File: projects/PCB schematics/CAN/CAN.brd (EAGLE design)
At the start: 160 x 100 mm, 0 parts

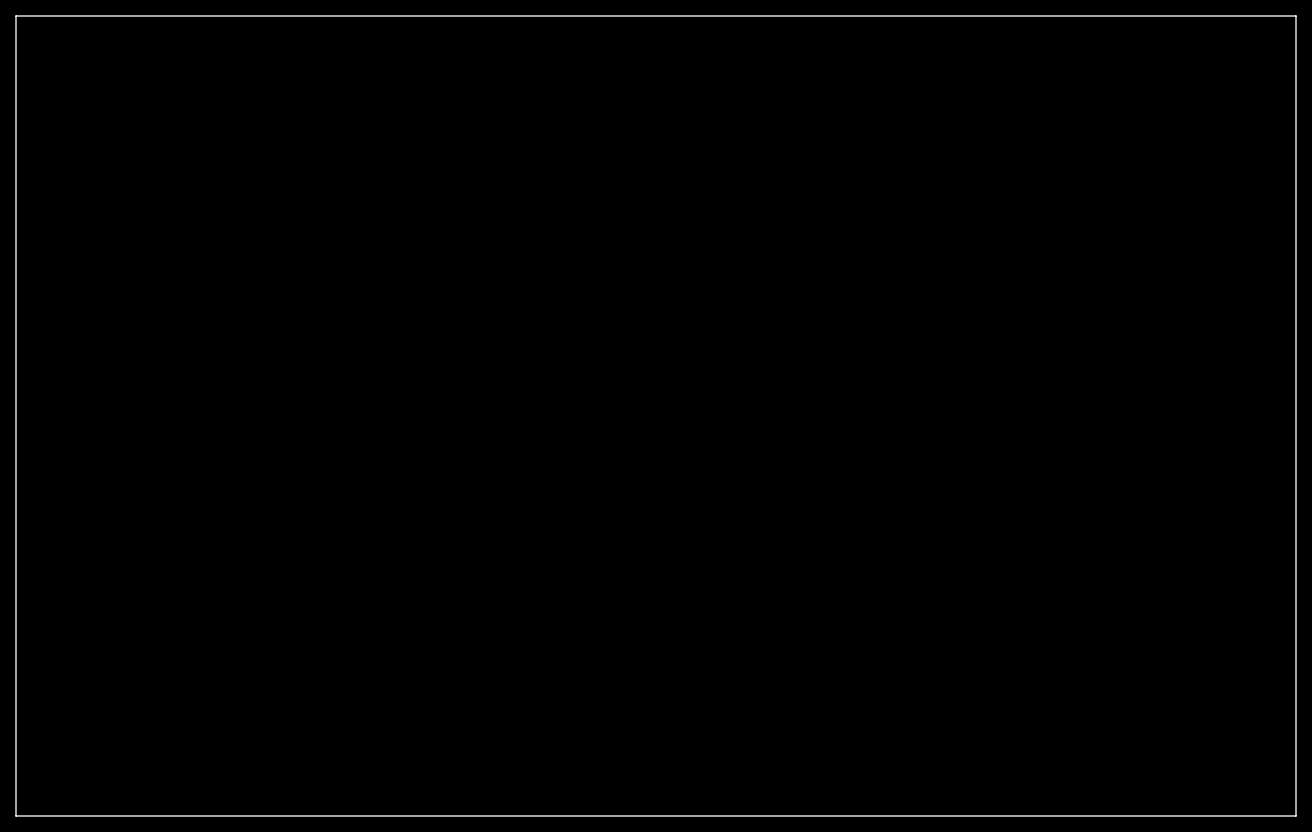
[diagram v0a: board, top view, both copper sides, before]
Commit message: CAN - Initial draft.
Vertical connectors chosen. Several options should be compliant with this PCB footprint.
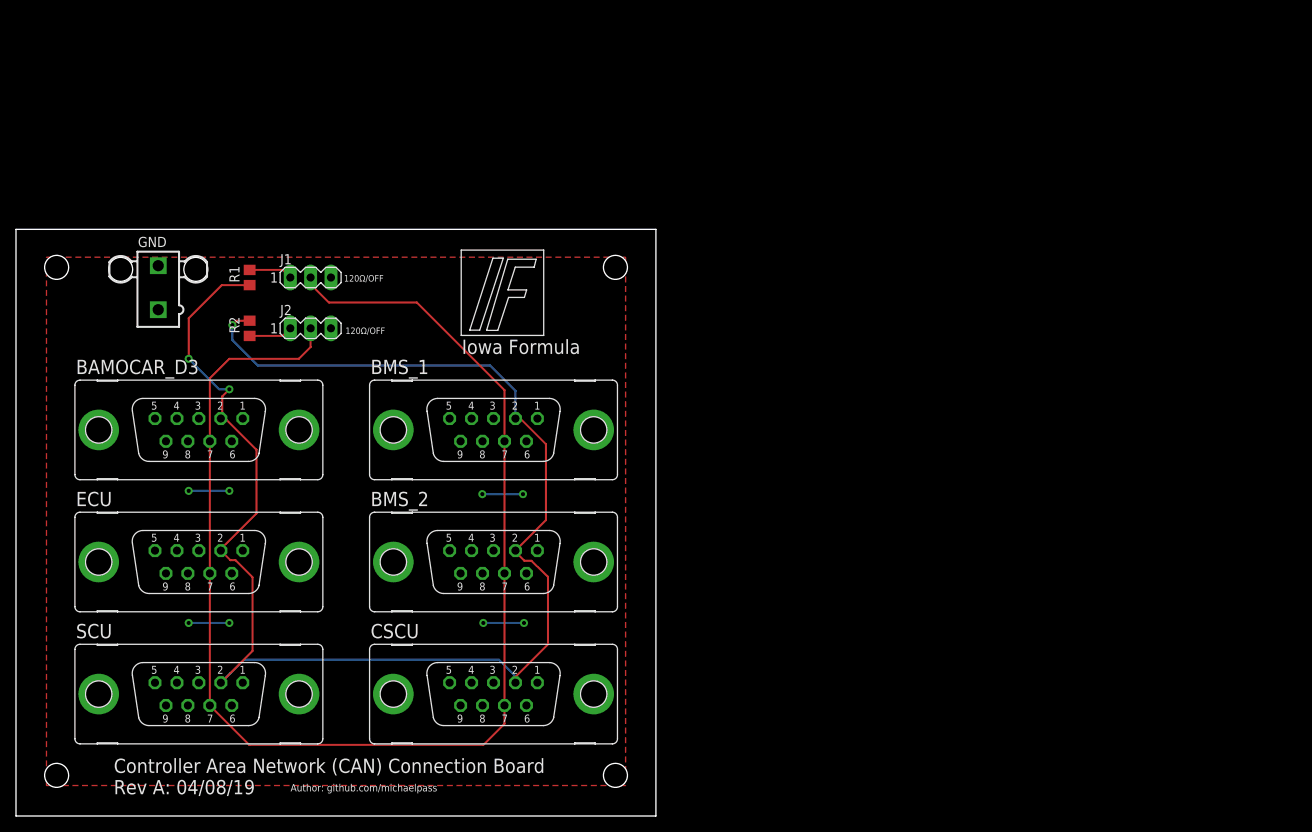
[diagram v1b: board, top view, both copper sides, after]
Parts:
- added BAMOCAR_D3, BMS_1, BMS_2, CSCU, ECU, SCU: (no value), con-subd:F09VP
- added GND: 5566-2, con-molex:5566-2
- added J1, J2: (no value), con-lstb:MA03-1
- added R1, R2: (no value), rcl:R0805
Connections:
- new net CANH: BAMOCAR_D3.7, BMS_1.7, BMS_2.7, CSCU.7, ECU.7, J1.2, J2.2, SCU.7
- new net CANL: BAMOCAR_D3.2, BMS_1.2, BMS_2.2, CSCU.2, ECU.2, R1.2, R2.2, SCU.2
- new net GND: BAMOCAR_D3.3, BAMOCAR_D3.6, BMS_1.3, BMS_1.6, BMS_2.3, BMS_2.6, CSCU.3, CSCU.6, ECU.3, ECU.6, GND.1, GND.2, SCU.3, SCU.6
- new net N$2: J2.3
- new net N$3: J2.1, R2.1
- new net N$4: J1.1, R1.1
- new net N$6: J1.3
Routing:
- net CANL: track 0.00 -> 191.8 mm, vias 0 -> 3
- net CANH: track 0.00 -> 169.7 mm
- net GND: track 0.00 -> 20.3 mm, vias 0 -> 8
- net N$4: track 0.00 -> 5.47 mm
- net N$3: track 0.00 -> 5.47 mm
- added copper zone on layer 1, net GND
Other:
- board size 160 x 100 mm -> 80 x 73.3 mm
- board text added: "120Ω/OFF"
- board text added: "Author: github.com/michaelpass"
- board text added: "Controller Area Network (CAN) Connection Board Rev A: 04/08/19"
- board text added: "Iowa Formula"

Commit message: CAN - Added in resistor values.
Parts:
- R1, R2: value (none) -> 120
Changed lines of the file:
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@@
 <attribute name="VALUE" x="33.02" y="58.039" size="1.27" layer="27" ratio="10"/>
 </element>
-<element name="R1" library="rcl" library_urn="urn:adsk.eagle:library:334" package="R0805" package3d_urn="urn:adsk.eagle:package:23553/2" value="" x="29.21" y="67.31" smashed="yes" rot="R270">
+<element name="R1" library="rcl" library_urn="urn:adsk.eagle:library:334" package="R0805" package3d_urn="urn:adsk.eagle:package:23553/2" value="120" x="29.21" y="67.31" smashed="yes" rot="R270">
 <attribute name="NAME" x="27.94" y="66.675" size="1.27" layer="25" rot="R90"/>
 <attribute name="SPICEPREFIX" value="R" x="29.21" y="67.31" size="1.778" layer="27" rot="R270" display="off"/>
 <attribute name="VALUE" x="26.67" y="67.945" size="1.27" layer="27" rot="R270"/>
 </element>
-<element name="R2" library="rcl" library_urn="urn:adsk.eagle:library:334" package="R0805" package3d_urn="urn:adsk.eagle:package:23553/2" value="" x="29.21" y="60.96" smashed="yes" rot="R90">
+<element name="R2" library="rcl" library_urn="urn:adsk.eagle:library:334" package="R0805" package3d_urn="urn:adsk.eagle:package:23553/2" value="120" x="29.21" y="60.96" smashed="yes" rot="R90">
 <attribute name="NAME" x="27.94" y="60.325" size="1.27" layer="25" rot="R90"/>
 <attribute name="SPICEPREFIX" value="R" x="29.21" y="60.96" size="1.778" layer="27" rot="R90" display="off"/>

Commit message: TSAL - Resizing.
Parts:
- moved SCU 15.3 mm to (33.0, 26.7)
- moved BAMOCAR_D3 15.3 mm to (33.0, 59.7)
- moved ECU 15.3 mm to (33.0, 43.2)
- moved J2 15.3 mm to (47.0, 72.4)
- moved CSCU 15.3 mm to (69.8, 26.7)
- moved J1 15.3 mm to (47.0, 78.7)
- moved BMS_1 15.3 mm to (69.8, 59.7)
- moved BMS_2 15.3 mm to (69.8, 43.2)
- moved R2 15.3 mm to (39.4, 72.4)
- moved GND 15.3 mm to (27.9, 77.5)
- moved R1 15.3 mm to (39.4, 78.7)
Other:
- board size 80 x 73.3 mm -> 99.1 x 99.1 mm

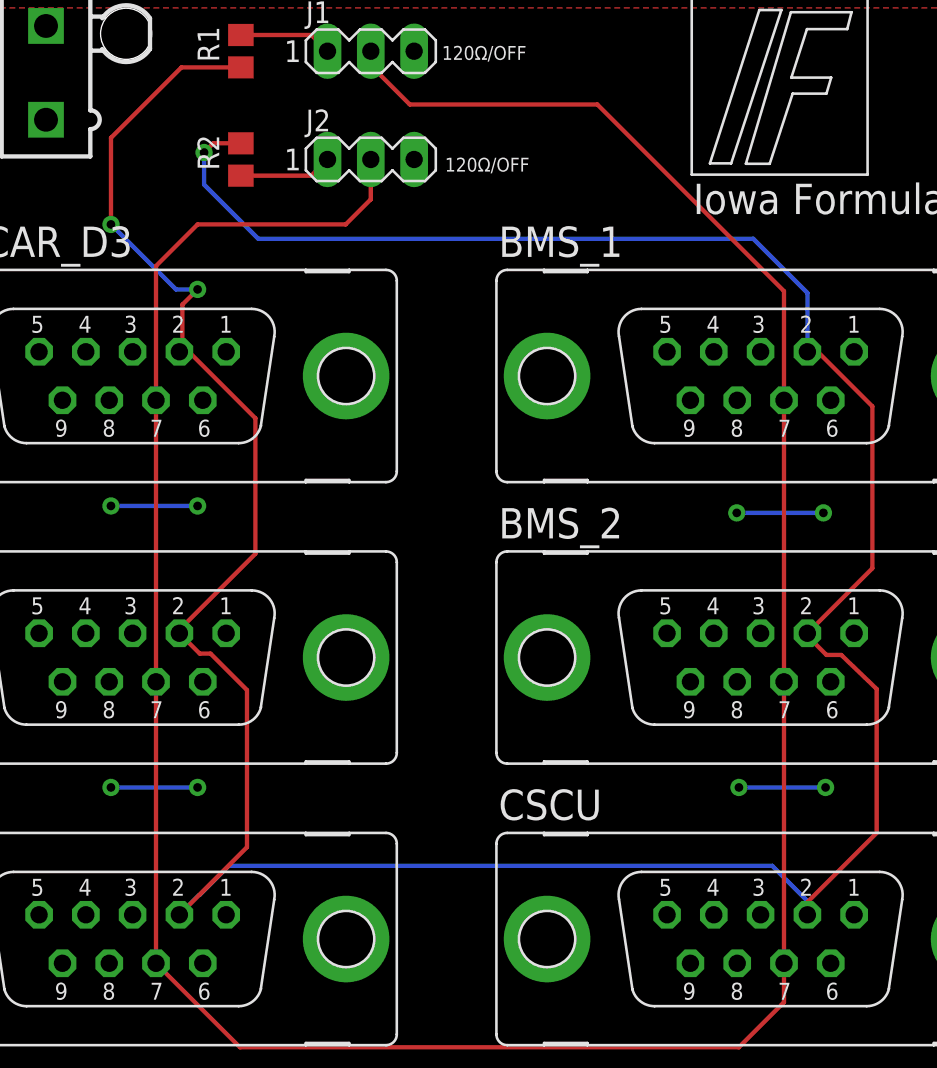
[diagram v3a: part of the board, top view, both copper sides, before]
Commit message: CAN - Further distancing of CAN_H/CAN_L routing.
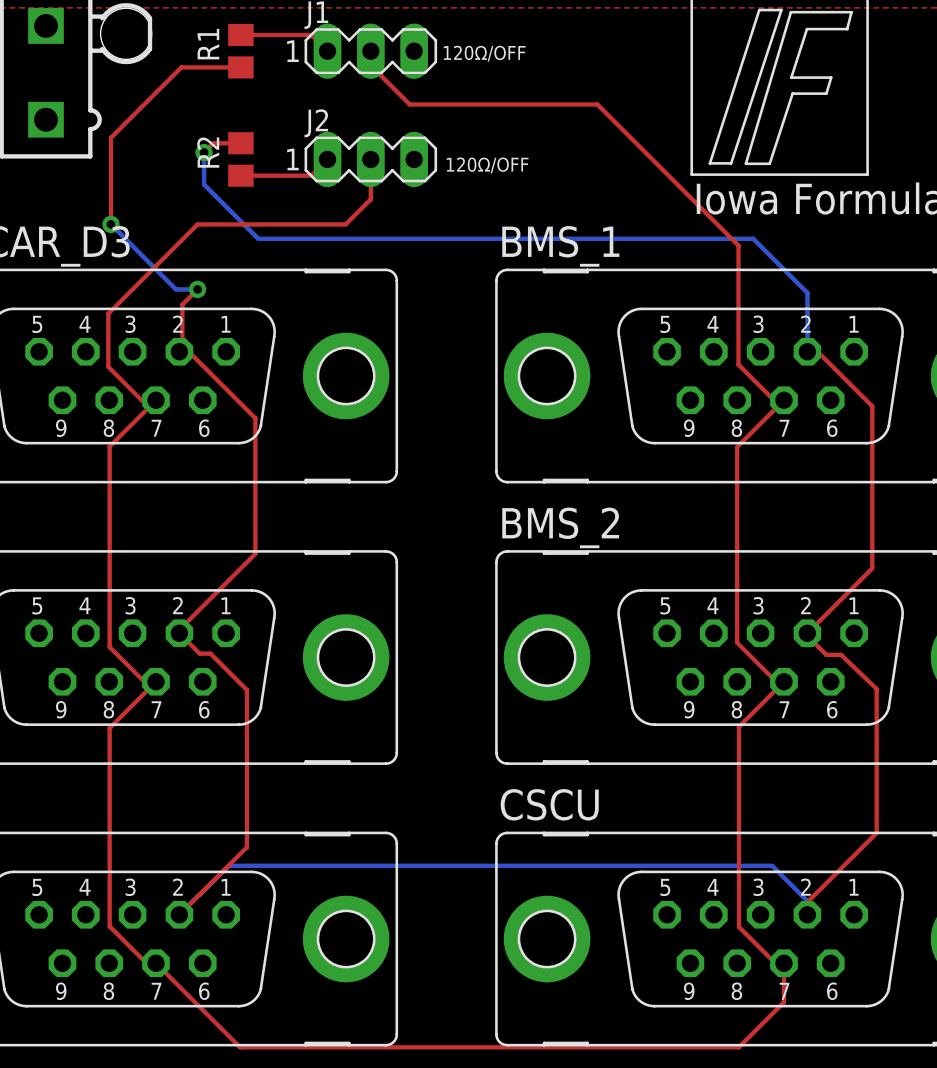
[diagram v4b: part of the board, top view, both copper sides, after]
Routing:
- net GND: track 20.3 -> 0.00 mm, vias 8 -> 0
- net CANH: track 169.7 -> 183.1 mm
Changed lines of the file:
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@@
 <contactref element="BMS_2" pad="6"/>
 <contactref element="BMS_2" pad="3"/>
-<via x="36.83" y="52.07" extent="1-16" drill="0.508"/>
-<via x="31.75" y="52.07" extent="1-16" drill="0.508"/>
-<wire x1="31.75" y1="52.07" x2="36.83" y2="52.07" width="0.254" layer="16"/>
-<via x="73.66" y="35.56" extent="1-16" drill="0.508"/>
-<via x="68.58" y="35.56" extent="1-16" drill="0.508"/>
-<wire x1="68.58" y1="35.56" x2="73.66" y2="35.56" width="0.254" layer="16"/>
-<via x="73.533" y="51.6636" extent="1-16" drill="0.508"/>
-<via x="68.453" y="51.6636" extent="1-16" drill="0.508"/>
-<wire x1="68.453" y1="51.6636" x2="73.533" y2="51.6636" width="0.254" layer="16"/>
-<via x="36.83" y="35.56" extent="1-16" drill="0.508"/>
-<via x="31.75" y="35.56" extent="1-16" drill="0.508"/>
-<wire x1="31.75" y1="35.56" x2="36.83" y2="35.56" width="0.254" layer="16"/>
 </signal>
 <signal name="N$2">
@@
 <contactref element="SCU" pad="7"/>
 <contactref element="CSCU" pad="7"/>
-<wire x1="34.3916" y1="58.2676" x2="34.3916" y2="41.7576" width="0.254" layer="1"/>
-<wire x1="34.3916" y1="41.7576" x2="34.3916" y2="25.2476" width="0.254" layer="1"/>
-<wire x1="71.2216" y1="41.7576" x2="71.2216" y2="58.2676" width="0.254" layer="1"/>
-<wire x1="71.2216" y1="25.2476" x2="71.2216" y2="41.7576" width="0.254" layer="1"/>
-<wire x1="34.3916" y1="58.2676" x2="34.3916" y2="66.1416" width="0.254" layer="1"/>
-<wire x1="34.3916" y1="66.1416" x2="36.83" y2="68.58" width="0.254" layer="1"/>
+<wire x1="34.3916" y1="58.2676" x2="31.6738" y2="55.5498" width="0.254" layer="1"/>
+<wire x1="31.6738" y1="55.5498" x2="31.6738" y2="43.7896" width="0.254" layer="1"/>
+<wire x1="33.7058" y1="41.7576" x2="34.3916" y2="41.7576" width="0.254" layer="1"/>
+<wire x1="33.7058" y1="41.7576" x2="31.6738" y2="43.7896" width="0.254" layer="1"/>
+<wire x1="34.3916" y1="41.7576" x2="31.6738" y2="39.0398" width="0.254" layer="1"/>
+<wire x1="31.6738" y1="39.0398" x2="31.6738" y2="27.4066" width="0.254" layer="1"/>
+<wire x1="33.8328" y1="25.2476" x2="31.6738" y2="27.4066" width="0.254" layer="1"/>
+<wire x1="33.8328" y1="25.2476" x2="34.3916" y2="25.2476" width="0.254" layer="1"/>
+<wire x1="71.2216" y1="41.7576" x2="70.7644" y2="41.7576" width="0.254" layer="1"/>
+<wire x1="70.7644" y1="41.7576" x2="68.4784" y2="44.0436" width="0.254" layer="1"/>
+<wire x1="68.4784" y1="55.5244" x2="68.4784" y2="44.0436" width="0.254" layer="1"/>
+<wire x1="68.4784" y1="55.5244" x2="71.2216" y2="58.2676" width="0.254" layer="1"/>
+<wire x1="71.2216" y1="25.2476" x2="70.7136" y2="25.2476" width="0.254" layer="1"/>
+<wire x1="70.7136" y1="25.2476" x2="68.58" y2="27.3812" width="0.254" layer="1"/>
+<wire x1="68.58" y1="39.116" x2="68.58" y2="27.3812" width="0.254" layer="1"/>
+<wire x1="68.58" y1="39.116" x2="71.2216" y2="41.7576" width="0.254" layer="1"/>
+<wire x1="34.3916" y1="58.2676" x2="33.5534" y2="58.2676" width="0.254" layer="1"/>
+<wire x1="33.5534" y1="58.2676" x2="31.5976" y2="60.2234" width="0.254" layer="1"/>
+<wire x1="31.5976" y1="63.3476" x2="31.5976" y2="60.2234" width="0.254" layer="1"/>
+<wire x1="31.5976" y1="63.3476" x2="36.83" y2="68.58" width="0.254" layer="1"/>
 <wire x1="36.83" y1="68.58" x2="45.5168" y2="68.58" width="0.254" layer="1"/>
 <wire x1="46.99" y1="72.39" x2="46.99" y2="70.0532" width="0.254" layer="1"/>
 <wire x1="46.99" y1="70.0532" x2="45.5168" y2="68.58" width="0.254" layer="1"/>
-<wire x1="71.2216" y1="58.2676" x2="71.2216" y2="64.6684" width="0.254" layer="1"/>
+<wire x1="71.2216" y1="58.2676" x2="70.6374" y2="58.2676" width="0.254" layer="1"/>
+<wire x1="70.6374" y1="58.2676" x2="68.5546" y2="60.3504" width="0.254" layer="1"/>
+<wire x1="68.5546" y1="67.3354" x2="68.5546" y2="60.3504" width="0.254" layer="1"/>
 <wire x1="60.2742" y1="75.6158" x2="49.276" y2="75.6158" width="0.254" layer="1"/>
 <wire x1="49.276" y1="75.6158" x2="46.99" y2="77.9018" width="0.254" layer="1"/>
 <wire x1="46.99" y1="77.9018" x2="46.99" y2="78.74" width="0.254" layer="1"/>
-<wire x1="71.2216" y1="64.6684" x2="60.2742" y2="75.6158" width="0.254" layer="1"/>
+<wire x1="68.5546" y1="67.3354" x2="60.2742" y2="75.6158" width="0.254" layer="1"/>
 <wire x1="34.3916" y1="25.2476" x2="39.3192" y2="20.32" width="0.254" layer="1"/>
 <wire x1="39.3192" y1="20.32" x2="68.58" y2="20.32" width="0.254" layer="1"/>
